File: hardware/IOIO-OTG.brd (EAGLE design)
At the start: 68.6 x 30.5 mm, 60 parts, among them Q1 IRLML2244, Q2 2N7002PW, Q3 AO3404A, U1 PIC24FJ256GB206, U14 SWITCH_SPDT, U2 TPS62133RGTT, U3 VREG_MIC5216

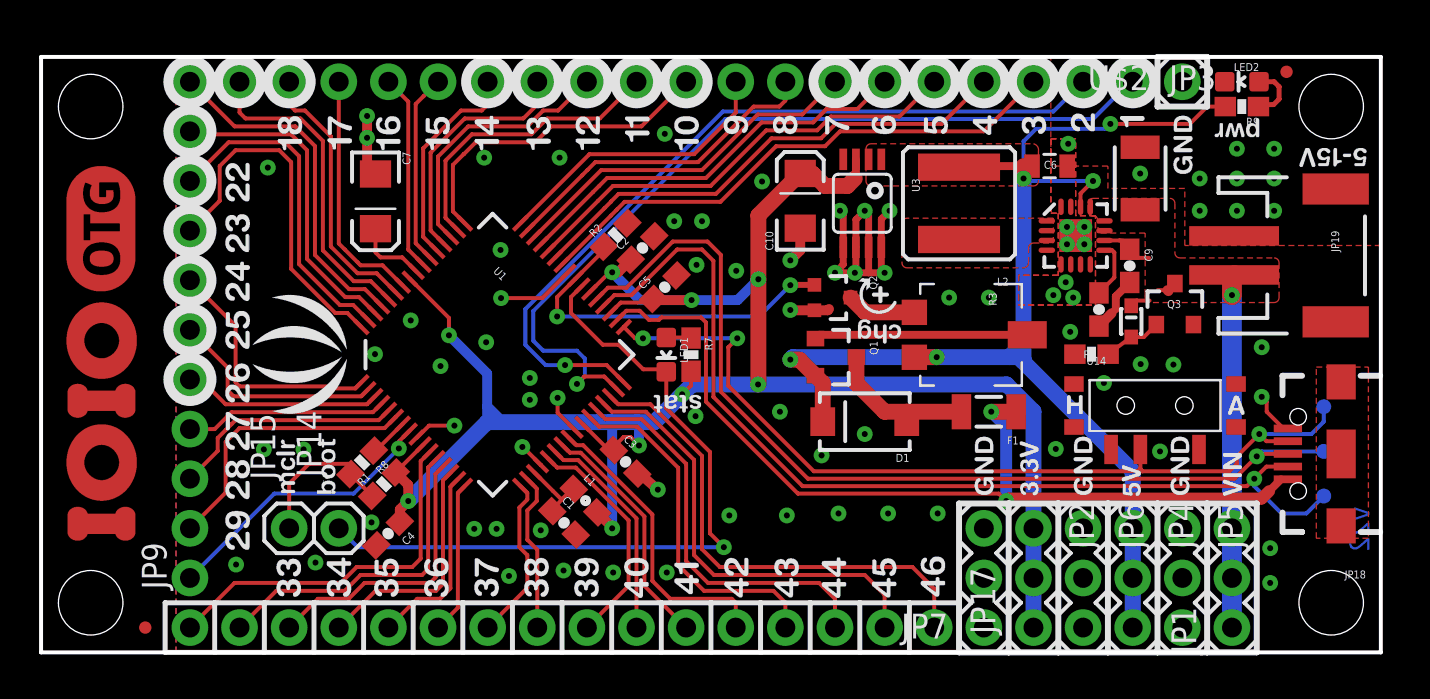
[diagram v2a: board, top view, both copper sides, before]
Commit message: Clearance errors
Set DRC to 7 mil (our standard is 8, but this design is really tight).
very slight shifting of some traces to fix clearance errors.
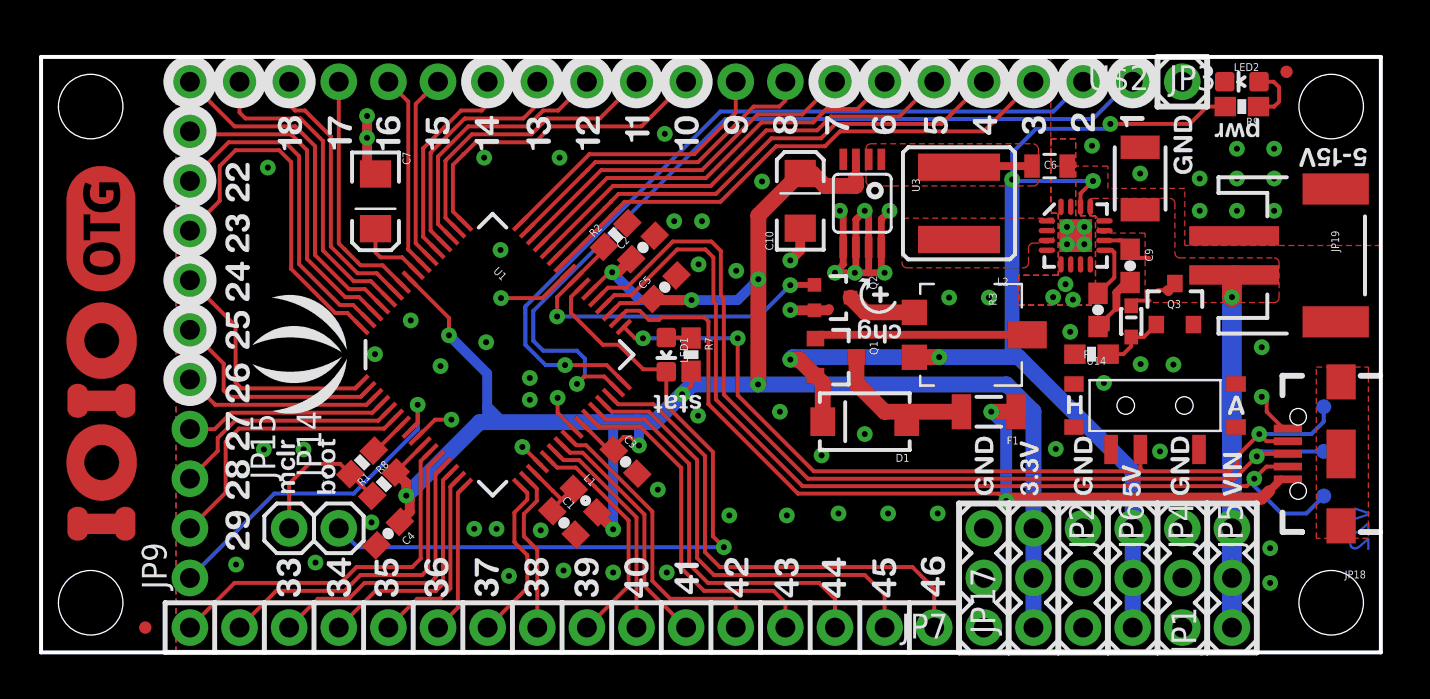
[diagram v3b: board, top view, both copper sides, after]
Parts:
- moved C8 0.05 mm to (54.1, 17.5)
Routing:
- net PIN30: track 14.6 -> 17.6 mm
- net GND: track 39.7 -> 38.2 mm
- net 3.3V: track 110.0 -> 111.1 mm
- net N$3: track 3.66 -> 3.04 mm
